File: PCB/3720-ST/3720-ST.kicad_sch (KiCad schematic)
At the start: 42 parts, among them J1 1546216-8, J10 1546216-8, J11 1546216-8, J12 1546216-8, J13 1546216-8, J14 1546216-8, J15 1546216-8, J16 1546216-8, J2 1546216-8, J3 1546216-8, J4 1546216-8, J5 1546216-8, J6 1546216-8, J7 1546216-8, J8 1546216-8, J9 1546216-8, U1 TMP275AID, U2 TMP275AID, U3 TMP275AID, U4 TMP275AID, U5 TMP275AID, U6 TMP275AID

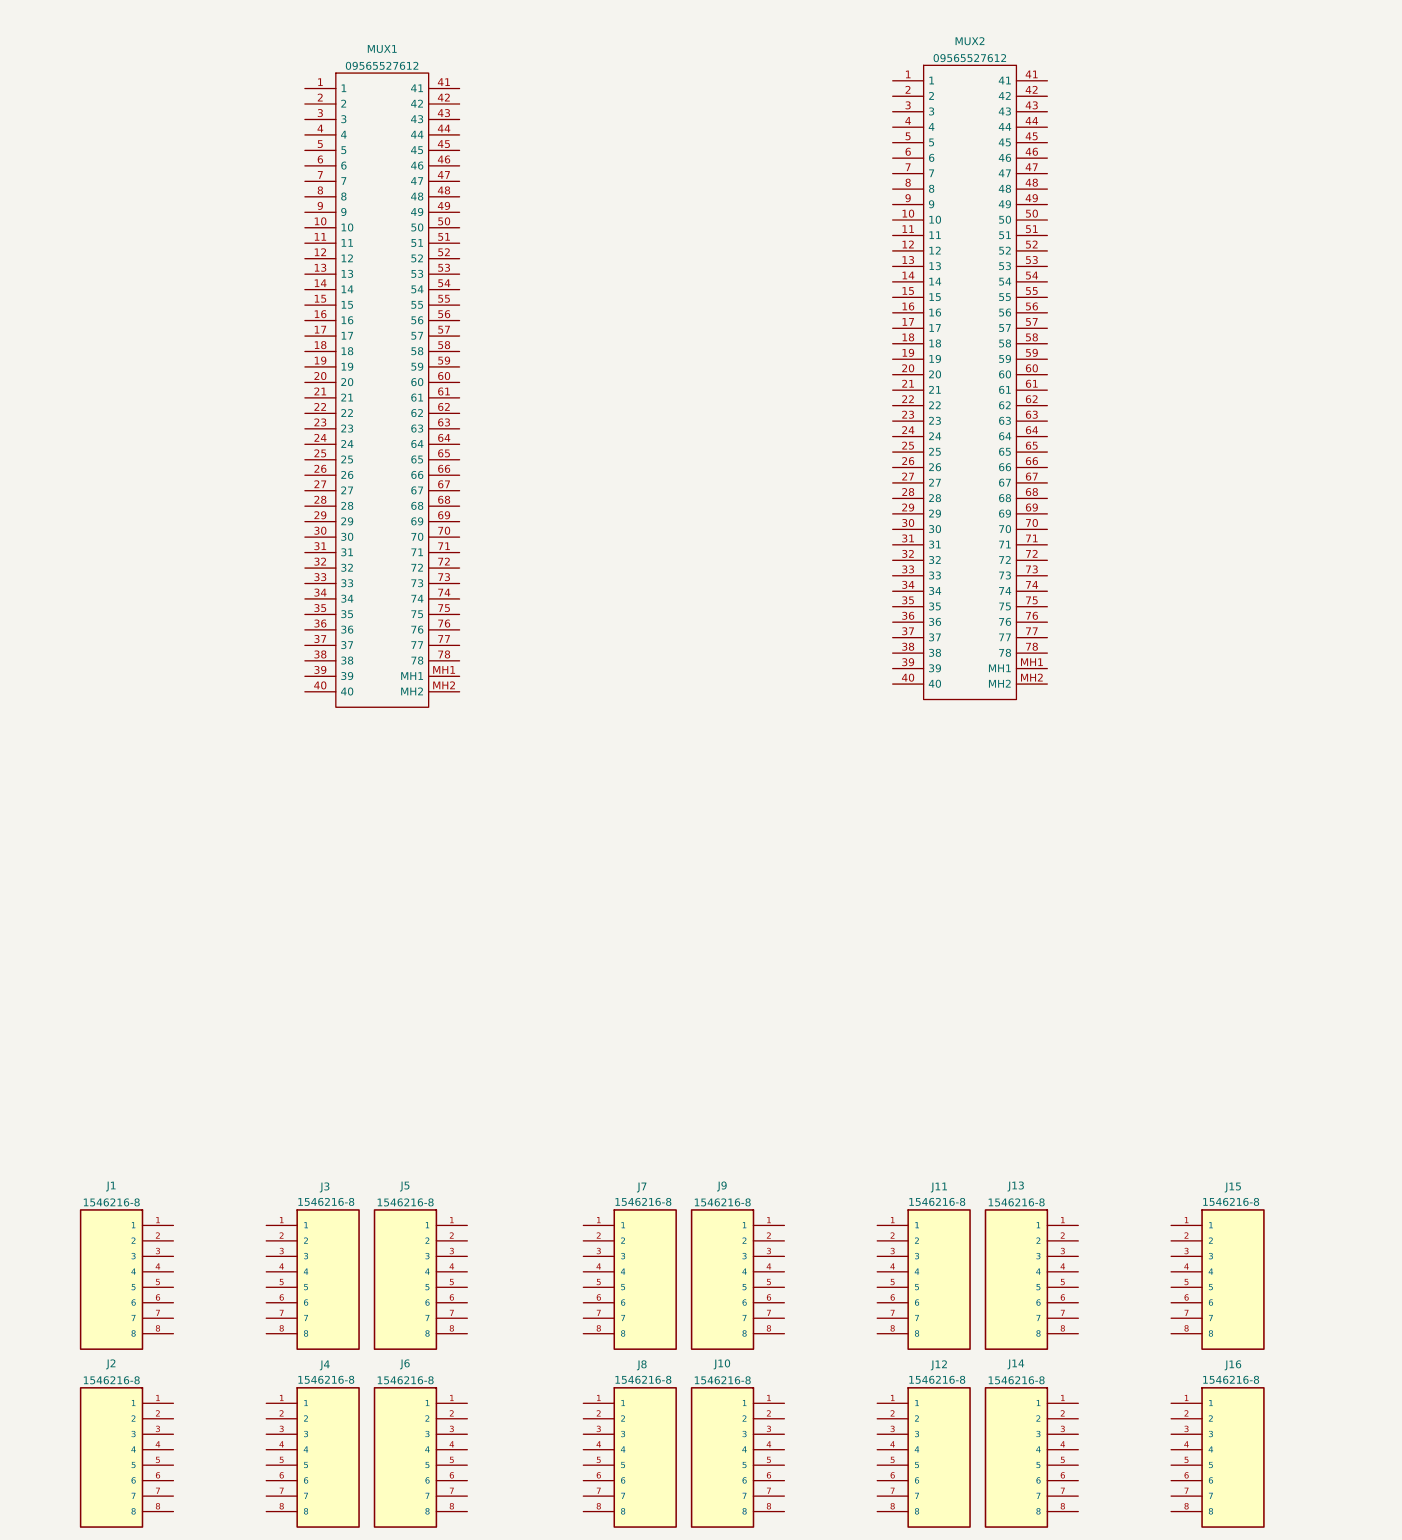
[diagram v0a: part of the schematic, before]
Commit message: Update 3720-ST.kicad_sch
updated pinout
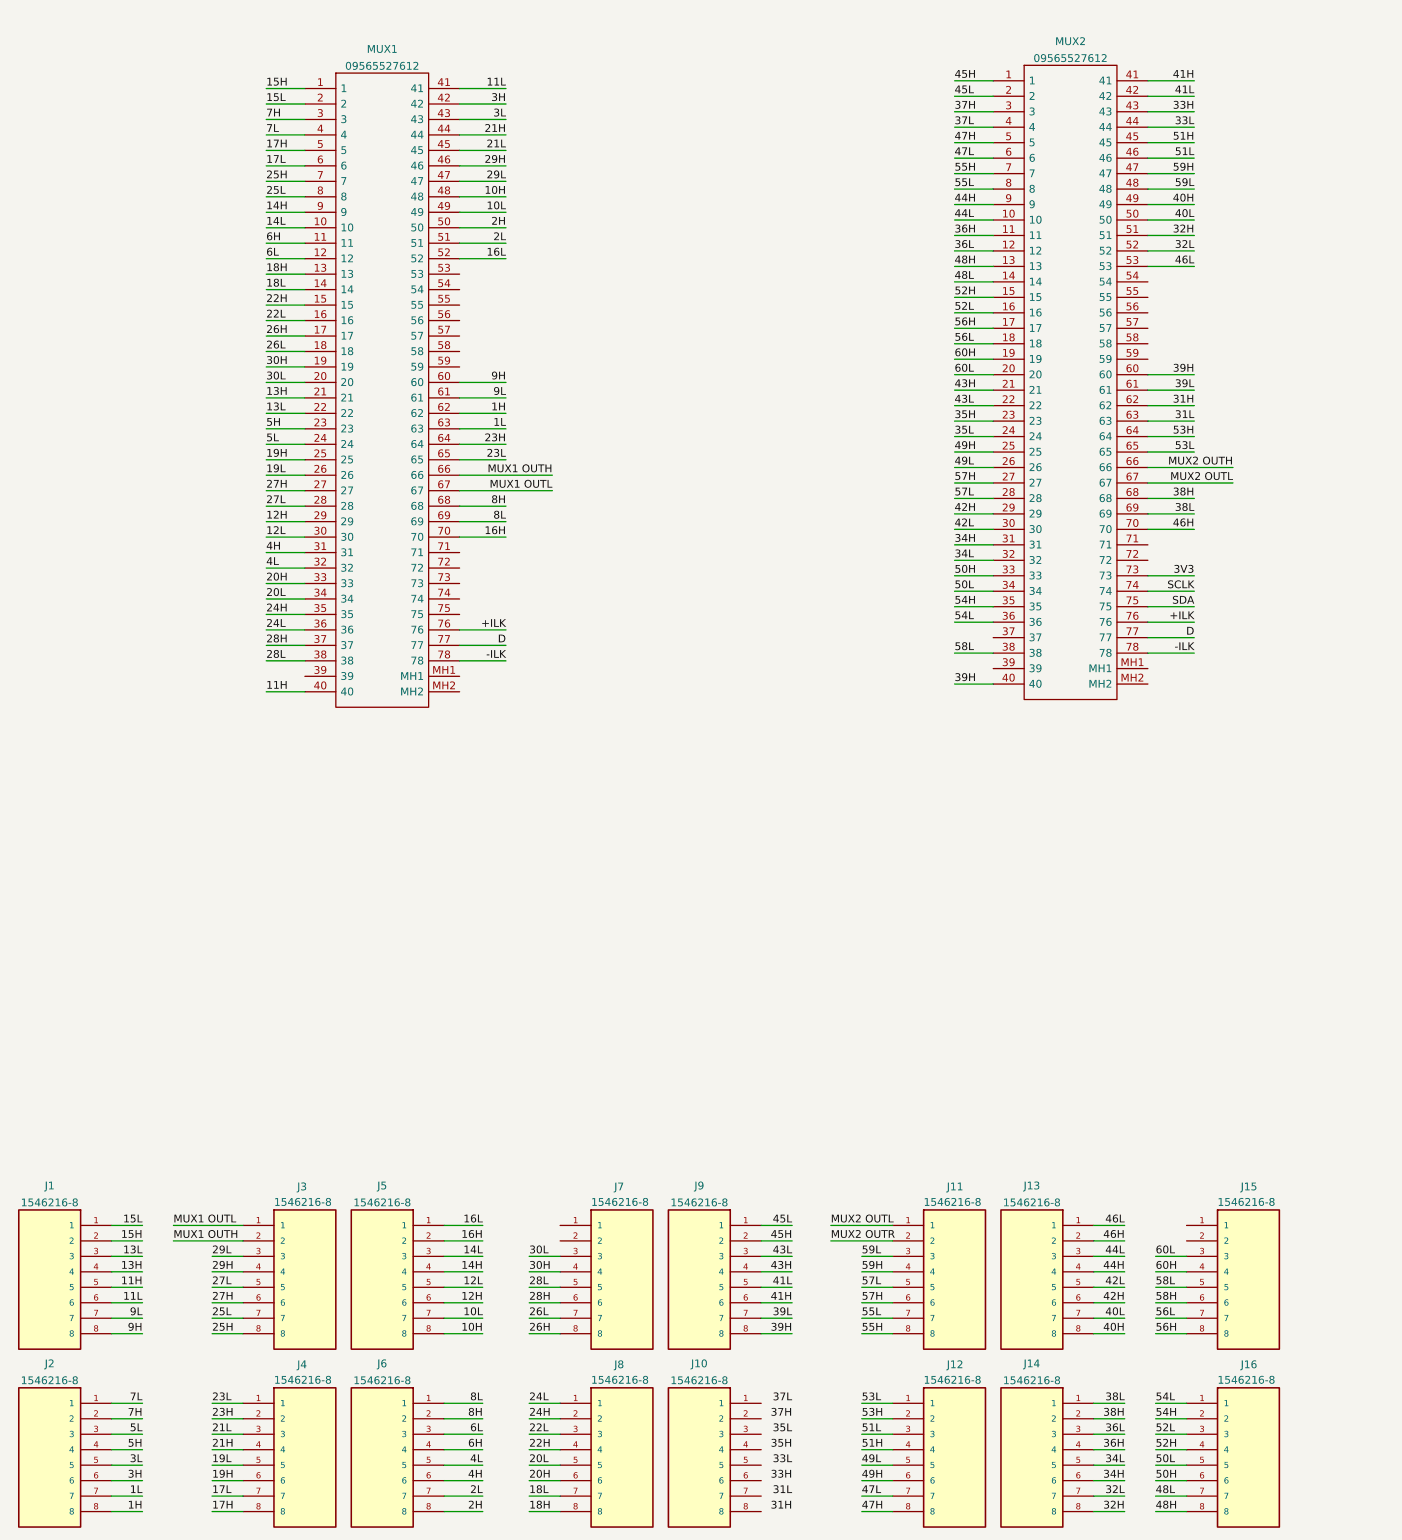
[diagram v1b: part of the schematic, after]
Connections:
- net SDA: now also MUX2.75
- net 15H: now reaches MUX1.1
- net 15H: now also J1.2
- net 14L: now reaches MUX1.10
- net 14L: now also J5.3
- net 6H: now reaches MUX1.11
- net 6H: now also J6.4
- net 6L: now reaches MUX1.12
- net 6L: now also J6.3
- net 18H: now reaches MUX1.13
- net 18H: now also J8.8
- net 18L: now reaches MUX1.14
- net 18L: now also J8.7
- net 22H: now reaches MUX1.15
- net 22H: now also J8.4
- net 22L: now reaches MUX1.16
- net 22L: now also J8.3
- net 26H: now reaches MUX1.17
- net 26H: now also J7.8
- net 26L: now reaches MUX1.18
- net 26L: now also J7.7
- net 30H: now reaches MUX1.19
- net 30H: now also J7.4
- net 15L: now reaches MUX1.2
- net 15L: now also J1.1
- net 30L: now reaches MUX1.20
- net 30L: now also J7.3
- net 13H: now reaches MUX1.21
- net 13H: now also J1.4
- net 13L: now reaches MUX1.22
- net 13L: now also J1.3
- net 5H: now reaches MUX1.23
- net 5H: now also J2.4
- net 5L: now reaches MUX1.24
- net 5L: now also J2.3
- net 19H: now reaches MUX1.25
- net 19H: now also J4.6
- net 19L: now reaches MUX1.26
- net 19L: now also J4.5
- net 27H: now reaches MUX1.27
- net 27H: now also J3.6
- net 27L: now reaches MUX1.28
- net 27L: now also J3.5
- net 12H: now reaches MUX1.29
- net 12H: now also J5.6
- net 7H: now reaches MUX1.3
- net 7H: now also J2.2
- net 12L: now reaches MUX1.30
- net 12L: now also J5.5
- net 4H: now reaches MUX1.31
- net 4H: now also J6.6
- net 4L: now reaches MUX1.32
- net 4L: now also J6.5
- net 20H: now reaches MUX1.33
- net 20H: now also J8.6
- net 20L: now reaches MUX1.34
- net 20L: now also J8.5
- net 24H: now reaches MUX1.35
- net 24H: now also J8.2
- net 24L: now reaches MUX1.36
- net 24L: now also J8.1
- net 28H: now reaches MUX1.37
- net 28H: now also J7.6
- net 28L: now reaches MUX1.38
- net 28L: now also J7.5
- net 7L: now reaches MUX1.4
- net 7L: now also J2.1
- net 11H: now reaches MUX1.40
- net 11H: now also J1.5
- net 11L: now reaches MUX1.41
- net 11L: now also J1.6
- net 3H: now reaches MUX1.42
- net 3H: now also J2.6
- net 3L: now reaches MUX1.43
- net 3L: now also J2.5
- net 21H: now reaches MUX1.44
- net 21H: now also J4.4
- net 21L: now reaches MUX1.45
- net 21L: now also J4.3
- net 29H: now reaches MUX1.46
- net 29H: now also J3.4
- net 29L: now reaches MUX1.47
- net 29L: now also J3.3
- net 10H: now reaches MUX1.48
- net 10H: now also J5.8
- net 10L: now reaches MUX1.49
- net 10L: now also J5.7
- net 17H: now reaches MUX1.5
- net 17H: now also J4.8
- net 2H: now reaches MUX1.50
- net 2H: now also J6.8
- net 2L: now reaches MUX1.51
- net 2L: now also J6.7
- net 16L: now reaches MUX1.52
- net 16L: now also J5.1
- net 17L: now reaches MUX1.6
- net 17L: now also J4.7
- net 9H: now reaches MUX1.60
- net 9H: now also J1.8
- net 9L: now reaches MUX1.61
- net 9L: now also J1.7
- net 1H: now reaches MUX1.62
- net 1H: now also J2.8
- net 1L: now reaches MUX1.63
- net 1L: now also J2.7
- net 23H: now reaches MUX1.64
- net 23H: now also J4.2
- net 23L: now reaches MUX1.65
- net 23L: now also J4.1
- net MUX1 OUTH: now reaches MUX1.66
- net MUX1 OUTH: now also J3.2
- net MUX1 OUTL: now reaches MUX1.67
- net MUX1 OUTL: now also J3.1
- net 8H: now reaches MUX1.68
- net 8H: now also J6.2
- net 8L: now reaches MUX1.69
- net 8L: now also J6.1
- net 25H: now reaches MUX1.7
- net 25H: now also J3.8
- net 16H: now reaches MUX1.70
- net 16H: now also J5.2
- net +ILK: now reaches MUX1.76
- net +ILK: now also MUX2.76
- net D: now reaches MUX1.77
- net D: now also MUX2.77
- net -ILK: now reaches MUX1.78
- net -ILK: now also MUX2.78
- net 25L: now reaches MUX1.8
- net 25L: now also J3.7
- net 14H: now reaches MUX1.9
- net 14H: now also J5.4
- net 46L: now reaches J13.1
- net 46L: now also MUX2.53
- net 46H: now reaches J13.2
- net 46H: now also MUX2.70
- net 44L: now reaches J13.3
- net 44L: now also MUX2.10
- net 44H: now reaches J13.4
- net 44H: now also MUX2.9
- net 42L: now reaches J13.5
- net 42L: now also MUX2.30
- net 42H: now reaches J13.6
- net 42H: now also MUX2.29
- net 40L: now reaches J13.7
- net 40L: now also MUX2.50
- net 40H: now reaches J13.8
- net 40H: now also MUX2.49
- net 45H: now reaches MUX2.1
- net 45H: now also J9.2
- net 36H: now reaches MUX2.11
- net 36H: now also J14.4
- net 36L: now reaches MUX2.12
- net 36L: now also J14.3
- net 48H: now reaches MUX2.13
- net 48H: now also J16.8
- net 48L: now reaches MUX2.14
- net 48L: now also J16.7
- net 52H: now reaches MUX2.15
- net 52H: now also J16.4
- net 52L: now reaches MUX2.16
- net 52L: now also J16.3
- net 56H: now reaches MUX2.17
- net 56H: now also J15.8
- net 56L: now reaches MUX2.18
- net 56L: now also J15.7
- net 60H: now reaches MUX2.19
- net 60H: now also J15.4
- net 45L: now reaches MUX2.2
- net 45L: now also J9.1
- net 60L: now reaches MUX2.20
- net 60L: now also J15.3
- net 43H: now reaches MUX2.21
- net 43H: now also J9.4
- net 43L: now reaches MUX2.22
- net 43L: now also J9.3
- net 35H: now reaches MUX2.23
- net 35L: now reaches MUX2.24
- net 49H: now reaches MUX2.25
- net 49H: now also J12.6
- net 49L: now reaches MUX2.26
- net 49L: now also J12.5
- net 57H: now reaches MUX2.27
- net 57H: now also J11.6
- net 57L: now reaches MUX2.28
- net 57L: now also J11.5
- net 37H: now reaches MUX2.3
- net 34H: now reaches MUX2.31
- net 34H: now also J14.6
- net 34L: now reaches MUX2.32
- net 34L: now also J14.5
- net 50H: now reaches MUX2.33
- net 50H: now also J16.6
- net 50L: now reaches MUX2.34
- net 50L: now also J16.5
- net 54H: now reaches MUX2.35
- net 54H: now also J16.2
- net 54L: now reaches MUX2.36
- net 54L: now also J16.1
- net 58L: now reaches MUX2.38
- net 58L: now also J15.5
- net 37L: now reaches MUX2.4
- net 39H: now reaches MUX2.40
- net 39H: now also J9.8, MUX2.60
- net 41H: now reaches MUX2.41
- net 41H: now also J9.6
- net 41L: now reaches MUX2.42
- net 41L: now also J9.5
- net 33H: now reaches MUX2.43
- net 33L: now reaches MUX2.44
- net 51H: now reaches MUX2.45
- net 51H: now also J12.4
- net 51L: now reaches MUX2.46
- net 51L: now also J12.3
- net 59H: now reaches MUX2.47
- net 59H: now also J11.4
- net 59L: now reaches MUX2.48
- net 59L: now also J11.3
- net 47H: now reaches MUX2.5
- net 47H: now also J12.8
- net 32H: now reaches MUX2.51
- net 32H: now also J14.8
- net 32L: now reaches MUX2.52
- net 32L: now also J14.7
- net 47L: now reaches MUX2.6
- net 47L: now also J12.7
- net 39L: now reaches MUX2.61
- net 39L: now also J9.7
- net 31H: now reaches MUX2.62
- net 31L: now reaches MUX2.63
- net 53H: now reaches MUX2.64
- net 53H: now also J12.2
- net 53L: now reaches MUX2.65
- net 53L: now also J12.1
- net MUX2 OUTH: now reaches MUX2.66
- net MUX2 OUTL: now reaches MUX2.67
- net MUX2 OUTL: now also J11.1
- net 38H: now reaches MUX2.68
- net 38H: now also J14.2
- net 38L: now reaches MUX2.69
- net 38L: now also J14.1
- net 55H: now reaches MUX2.7
- net 55H: now also J11.8
- net 3V3: now reaches MUX2.73
- net SCLK: now reaches MUX2.74
- net 55L: now reaches MUX2.8
- net 55L: now also J11.7
- net 58H: now reaches J15.6
- net MUX2 OUTR: now reaches J11.2
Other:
- moved on the sheet: J1, J10, J11, J12, J13, J14, J15, J16, J2, J3, J4, J5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

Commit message: Finished layout
fixed layout and added dxf files
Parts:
- removed C3, C4: 100nF, symbol Device:C_Small
- removed R5, R6, R7, R8: 5K, Resistor_SMD:R_0805_2012Metric, symbol Device:R_Small_US
- removed U3, U4: TMP275AID, D8, symbol BVKSound:TMP275AID
- C1, C2, C5, C6: footprint (none) -> Capacitor_SMD:C_0805_2012Metric
- U1, U2: footprint D8 -> BVKSound:TMP275AID
- U3: renamed from U5; footprint D8 -> BVKSound:TMP275AID
- U4: renamed from U6; footprint D8 -> BVKSound:TMP275AID
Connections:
- net 31H: now also J10.8
- net 31L: now also J10.7
- net 33H: now also J10.6
- net 33L: now also J10.5
- net 35H: now also J10.4
- net 35L: now also J10.3
- net 37H: now also J10.2
- net 37L: now also J10.1
- net 58H: now also MUX2.37
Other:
- moved on the sheet: C5, C6, R10, R11, R12, R9, U3, U4

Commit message: final board layout before routing
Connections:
- net +ILK renamed ILK1
- net ILK1: now also MUX1.78; no longer MUX2.76
- net -ILK renamed ILK2
- net ILK2: now also MUX2.76; no longer MUX1.78
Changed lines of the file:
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@@
     (effects (font (size 1.27 1.27)) (justify right bottom))
   )
-  (label "+ILK" (at 213.36 116.84 180)
+  (label "ILK2" (at 213.36 116.84 180)
     (effects (font (size 1.27 1.27)) (justify right bottom))
   )
@@
     (effects (font (size 1.27 1.27)) (justify left bottom))
   )
-  (label "+ILK" (at 100.33 118.11 180)
+  (label "ILK1" (at 100.33 118.11 180)
     (effects (font (size 1.27 1.27)) (justify right bottom))
   )
@@
     (effects (font (size 1.27 1.27)) (justify right bottom))
   )
-  (label "-ILK" (at 100.33 123.19 180)
+  (label "ILK1" (at 100.33 123.19 180)
     (effects (font (size 1.27 1.27)) (justify right bottom))
   )
@@
     (effects (font (size 1.27 1.27)) (justify right bottom))
   )
-  (label "-ILK" (at 213.36 121.92 180)
-    (effects (font (size 1.27 1.27)) (justify right bottom))
-  )
+  (label "ILK2" (at 213.36 121.92 180)
+    (effects (font (size 1.27 1.27)) (justify right bottom))
+  )

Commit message: Design finished, ready for review
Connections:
- net 32H: now also MUX2.50; no longer MUX2.51
- net 32L: now also MUX2.51; no longer MUX2.52
- net 33H: now also MUX2.42; no longer MUX2.43
- net 33L: now also MUX2.43; no longer MUX2.44
- net 39H: no longer MUX2.40
- net 40H: now also MUX2.48; no longer MUX2.49
- net 40L: now also MUX2.49; no longer MUX2.50
- net 41H: now also MUX2.40; no longer MUX2.41
- net 41L: now also MUX2.41; no longer MUX2.42
- net 46L: now also MUX2.52; no longer MUX2.53
- net 51H: now also MUX2.44; no longer MUX2.45
- net 51L: now also MUX2.45; no longer MUX2.46
- net 59H: now also MUX2.46; no longer MUX2.47
- net 59L: now also MUX2.47; no longer MUX2.48
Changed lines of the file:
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@@
     (stroke (width 0) (type default) (color 0 0 0 0))
   )
-  (wire (pts (xy 205.74 58.42) (xy 213.36 58.42))
-    (stroke (width 0) (type default) (color 0 0 0 0))
-  )
   (wire (pts (xy 205.74 114.3) (xy 213.36 114.3))
     (stroke (width 0) (type default) (color 0 0 0 0))
@@
     (effects (font (size 1.27 1.27)) (justify left bottom))
   )
-  (label "32H" (at 213.36 53.34 180)
+  (label "32L" (at 213.36 53.34 180)
     (effects (font (size 1.27 1.27)) (justify right bottom))
   )
-  (label "51H" (at 213.36 38.1 180)
+  (label "51L" (at 213.36 38.1 180)
     (effects (font (size 1.27 1.27)) (justify right bottom))
   )
@@
     (effects (font (size 1.27 1.27)) (justify right bottom))
   )
-  (label "51L" (at 213.36 40.64 180)
+  (label "59H" (at 213.36 40.64 180)
     (effects (font (size 1.27 1.27)) (justify right bottom))
   )
@@
     (effects (font (size 1.27 1.27)) (justify right bottom))
   )
-  (label "41H" (at 213.36 27.94 180)
+  (label "41L" (at 213.36 27.94 180)
     (effects (font (size 1.27 1.27)) (justify right bottom))
   )
@@
     (effects (font (size 1.27 1.27)) (justify right bottom))
   )
-  (label "33H" (at 213.36 33.02 180)
+  (label "33L" (at 213.36 33.02 180)
     (effects (font (size 1.27 1.27)) (justify right bottom))
   )
@@
     (effects (font (size 1.27 1.27)) (justify left bottom))
   )
-  (label "46L" (at 213.36 58.42 180)
-    (effects (font (size 1.27 1.27)) (justify right bottom))
-  )
   (label "29H" (at 100.33 41.91 180)
     (effects (font (size 1.27 1.27)) (justify right bottom))
@@
     (effects (font (size 1.27 1.27)) (justify right bottom))
   )
-  (label "40L" (at 213.36 50.8 180)
+  (label "32H" (at 213.36 50.8 180)
     (effects (font (size 1.27 1.27)) (justify right bottom))
   )
@@
     (effects (font (size 1.27 1.27)) (justify left bottom))
   )
-  (label "59H" (at 213.36 43.18 180)
+  (label "59L" (at 213.36 43.18 180)
     (effects (font (size 1.27 1.27)) (justify right bottom))
   )
@@
     (effects (font (size 1.27 1.27)) (justify left bottom))
   )
-  (label "33L" (at 213.36 35.56 180)
+  (label "51H" (at 213.36 35.56 180)
     (effects (font (size 1.27 1.27)) (justify right bottom))
   )
@@
     (effects (font (size 1.27 1.27)) (justify right bottom))
   )
-  (label "40H" (at 213.36 48.26 180)
+  (label "40L" (at 213.36 48.26 180)
     (effects (font (size 1.27 1.27)) (justify right bottom))
   )
@@
     (effects (font (size 1.27 1.27)) (justify left bottom))
   )
-  (label "41L" (at 213.36 30.48 180)
+  (label "33H" (at 213.36 30.48 180)
     (effects (font (size 1.27 1.27)) (justify right bottom))
   )
@@
     (effects (font (size 1.27 1.27)) (justify left bottom))
   )
-  (label "32L" (at 213.36 55.88 180)
+  (label "46L" (at 213.36 55.88 180)
     (effects (font (size 1.27 1.27)) (justify right bottom))
   )
@@
     (effects (font (size 1.27 1.27)) (justify left bottom))
   )
-  (label "59L" (at 213.36 45.72 180)
+  (label "40H" (at 213.36 45.72 180)
     (effects (font (size 1.27 1.27)) (justify right bottom))
   )
@@
     (effects (font (size 1.27 1.27)) (justify right bottom))
   )
-  (label "39H" (at 173.99 127 0)
+  (label "41H" (at 173.99 127 0)
     (effects (font (size 1.27 1.27)) (justify left bottom))
   )

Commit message: silkscreen added + fix in design
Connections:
- net 11H: now also J1.6; no longer J1.5
- net 11L: now also J1.5; no longer J1.6
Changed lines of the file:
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@@
     (effects (font (size 1.27 1.27)) (justify left bottom))
   )
-  (label "11L" (at 40.64 228.6 180)
+  (label "11H" (at 40.64 228.6 180)
     (effects (font (size 1.27 1.27)) (justify right bottom))
   )
@@
     (effects (font (size 1.27 1.27)) (justify left bottom))
   )
-  (label "11H" (at 40.64 226.06 180)
-    (effects (font (size 1.27 1.27)) (justify right bottom))
-  )
+  (label "11L" (at 40.64 226.06 180)
+    (effects (font (size 1.27 1.27)) (justify right bottom))
+  )
